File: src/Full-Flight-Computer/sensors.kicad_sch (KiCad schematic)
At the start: 11 parts, among them U12 BMM150, U3 BMI323, U5 BMP390

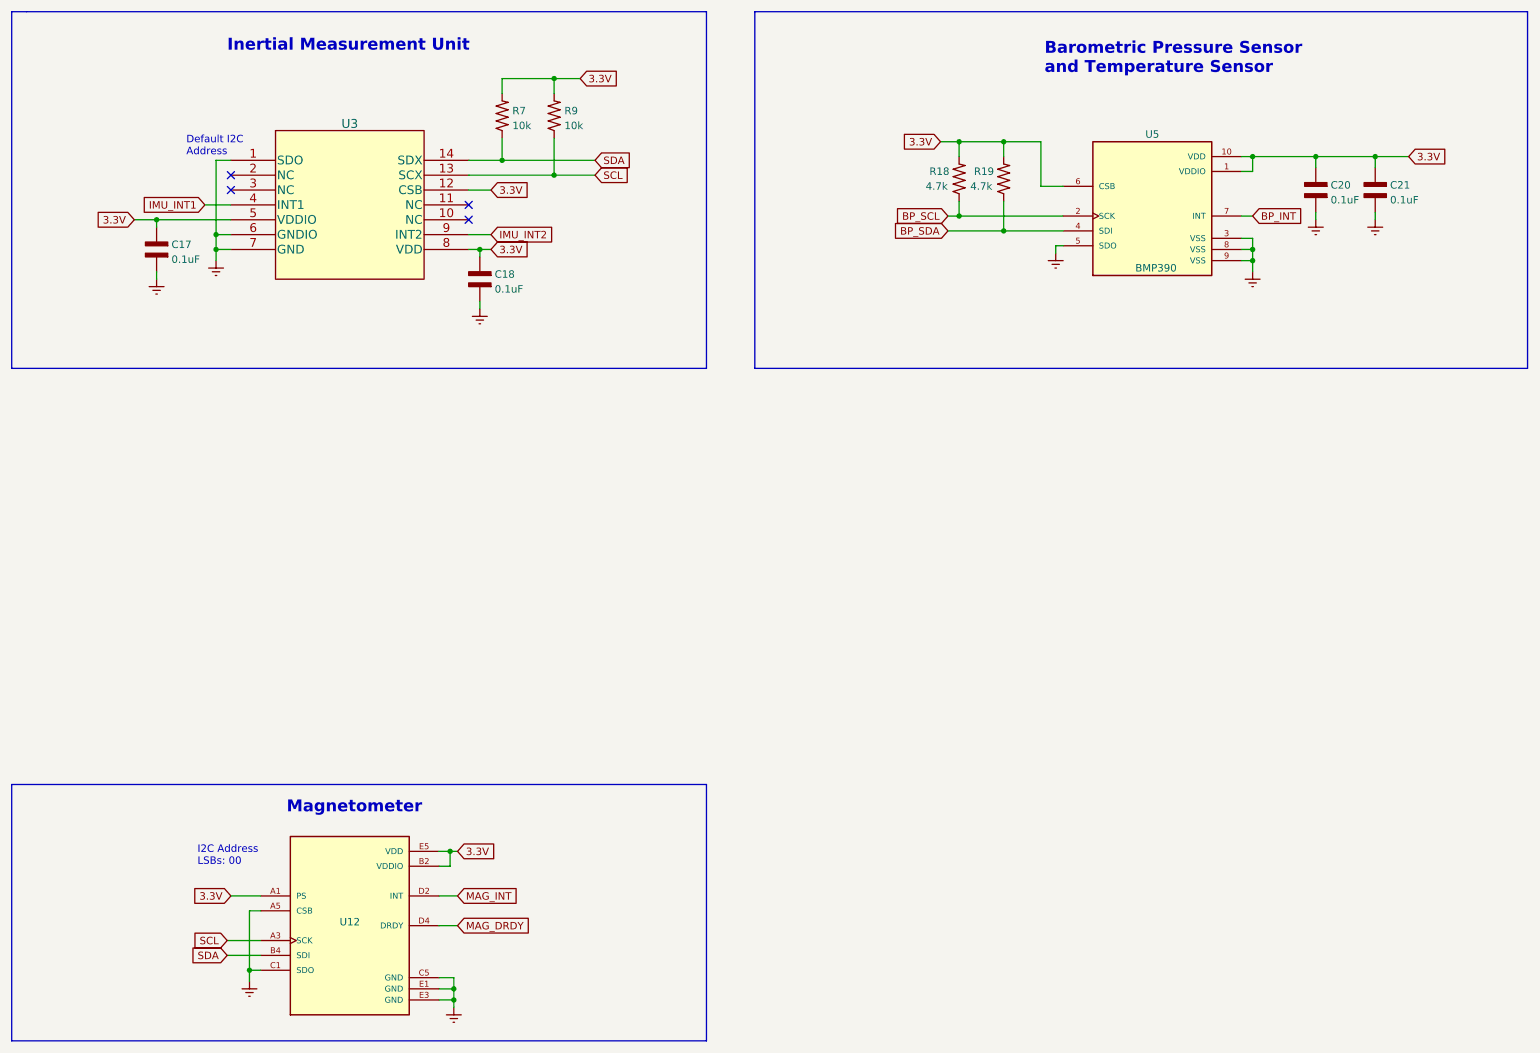
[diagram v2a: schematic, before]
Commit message: added auxiliary ports for staging/redundant ejection charges
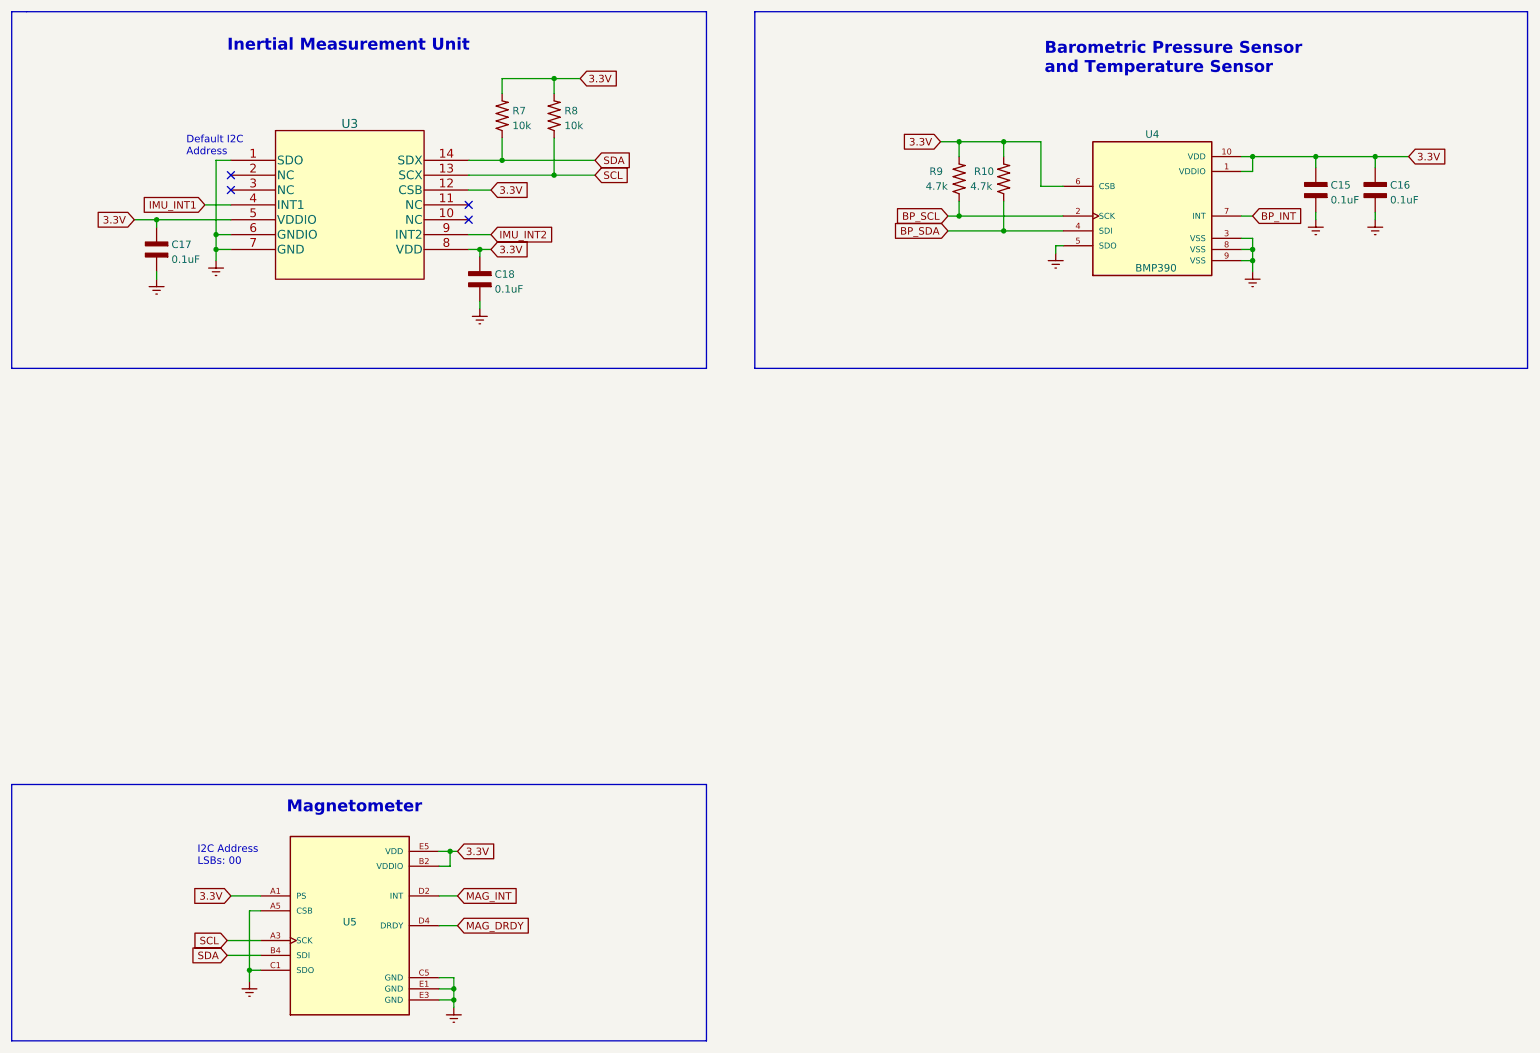
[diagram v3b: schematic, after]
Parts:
- renumbered C20 to C15, C21 to C16, R19 to R10, R9 to R8, R18 to R9, U5 to U4, U12 to U5

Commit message: implemented high G accelerometer schematic
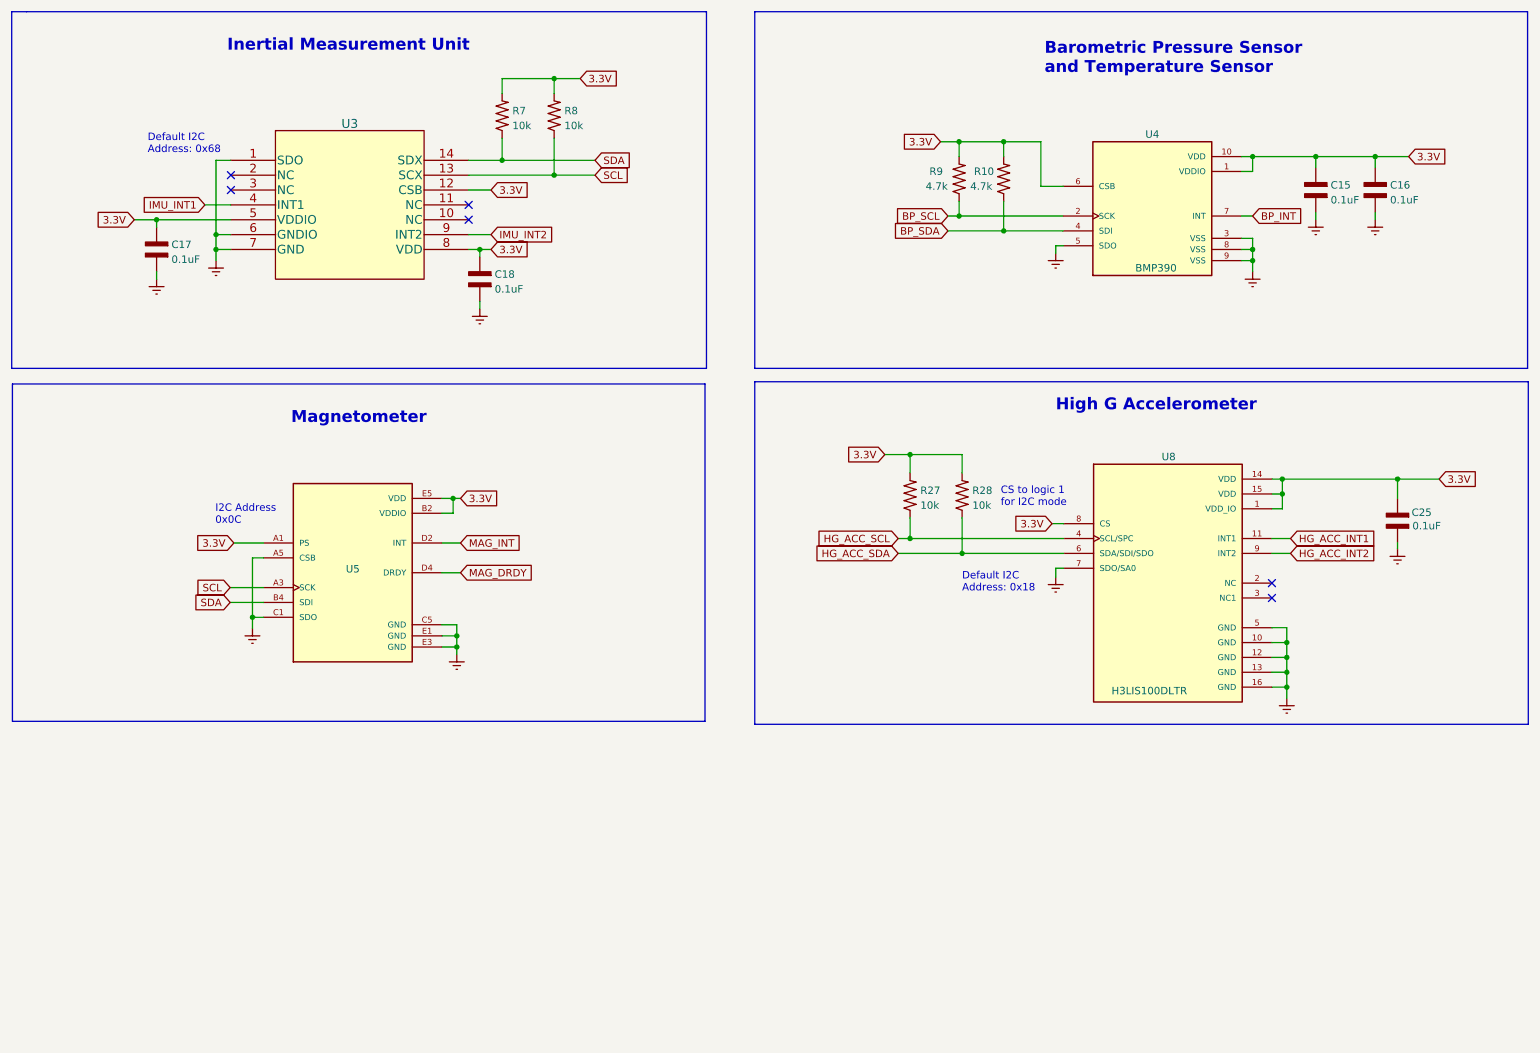
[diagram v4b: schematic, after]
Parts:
- added C25: 0.1uF, Full-Flight-Computer:CAP_0402, symbol Full-Flight-Computer:CAP_0402
- added R27, R28: 10k, Full-Flight-Computer:RES_0402, symbol Full-Flight-Computer:RES_0402
- added U8: H3LIS100DLTR, Full-Flight-Computer:H3LIS100DLTR, symbol Full-Flight-Computer:H3LIS100DLTR
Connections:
- net 3.3V: now also C25.1, R27.2, R28.2, U8.1 (VDD_IO), U8.14 (VDD), U8.15 (VDD), U8.8 (CS)
- net Earth: now also C25.2, U8.10 (GND), U8.12 (GND), U8.13 (GND), U8.16 (GND), U8.5 (GND), U8.7 (SDO/SA0)
- new net HG_ACC_INT1: U8.11 (INT1)
- new net HG_ACC_INT2: U8.9 (INT2)
- new net HG_ACC_SCL: R27.1, U8.4 (SCL/SPC)
- new net HG_ACC_SDA: R28.1, U8.6 (SDA/SDI/SDO)
- no-connect marks 4 -> 6
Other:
- note added: "CS to logic 1 for I2C mode"
- note added: "Default I2C Address: 0x18"
- note added: "Default I2C Address: 0x68"
- note added: "High G Accelerometer"
- note added: "I2C Address 0x0C"
- note removed: "Default I2C Address"
- note removed: "I2C Address LSBs: 00"
- moved on the sheet: U5

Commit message: redid component designators and updated BOM
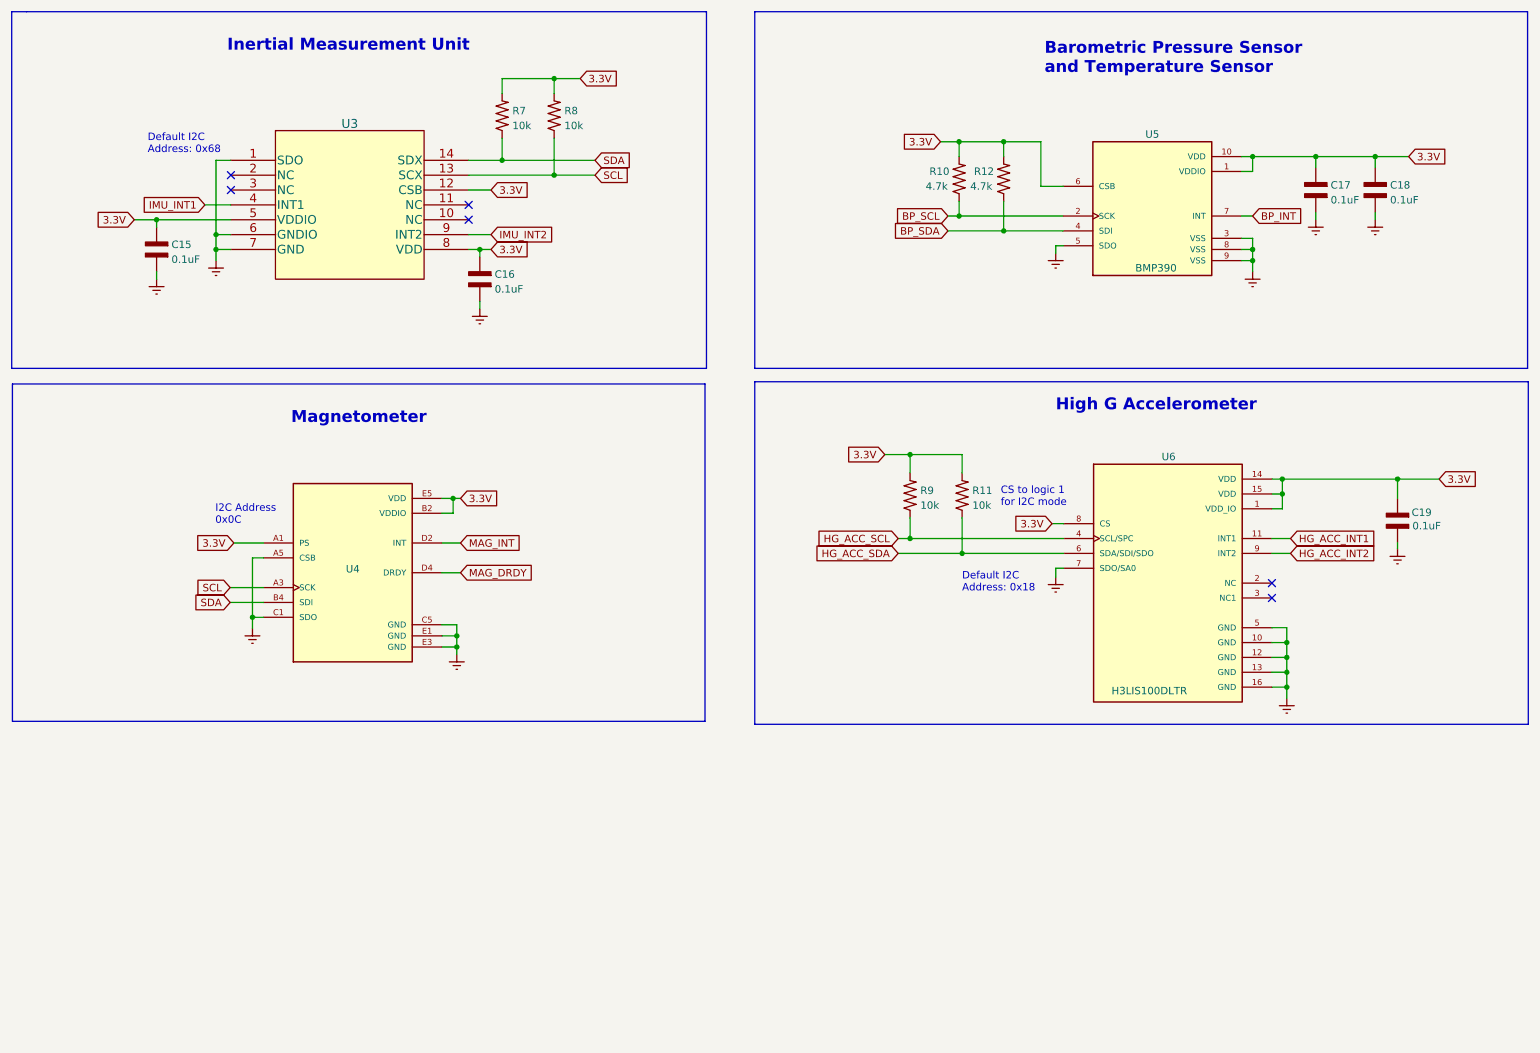
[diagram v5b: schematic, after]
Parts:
- renumbered C17 to C15, C18 to C16, C15 to C17, C16 to C18, C25 to C19, R9 to R10, R28 to R11, R10 to R12, R27 to R9, U5 to U4, U4 to U5, U8 to U6

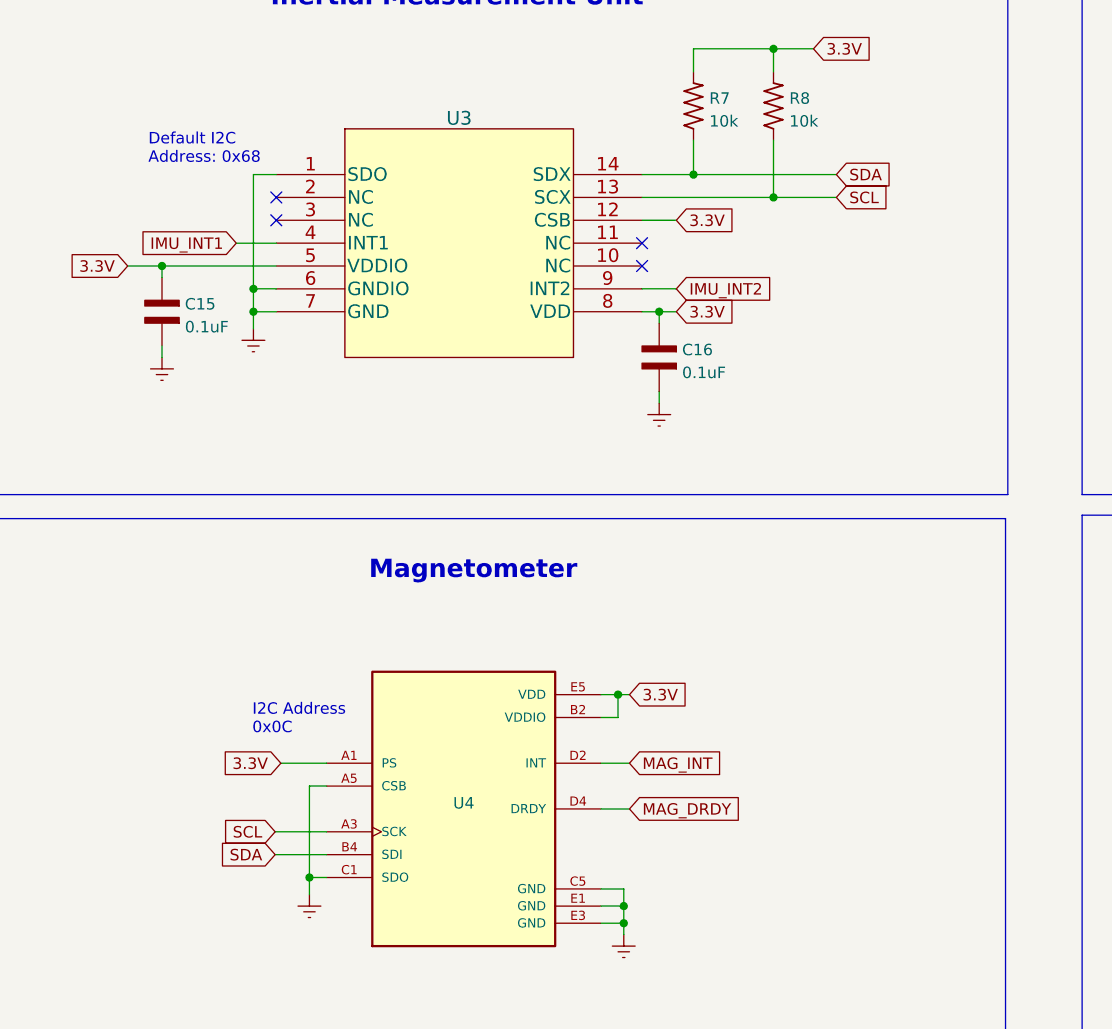
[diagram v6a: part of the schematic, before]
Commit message: add IMU prefix to IMU SDA and SCL labels
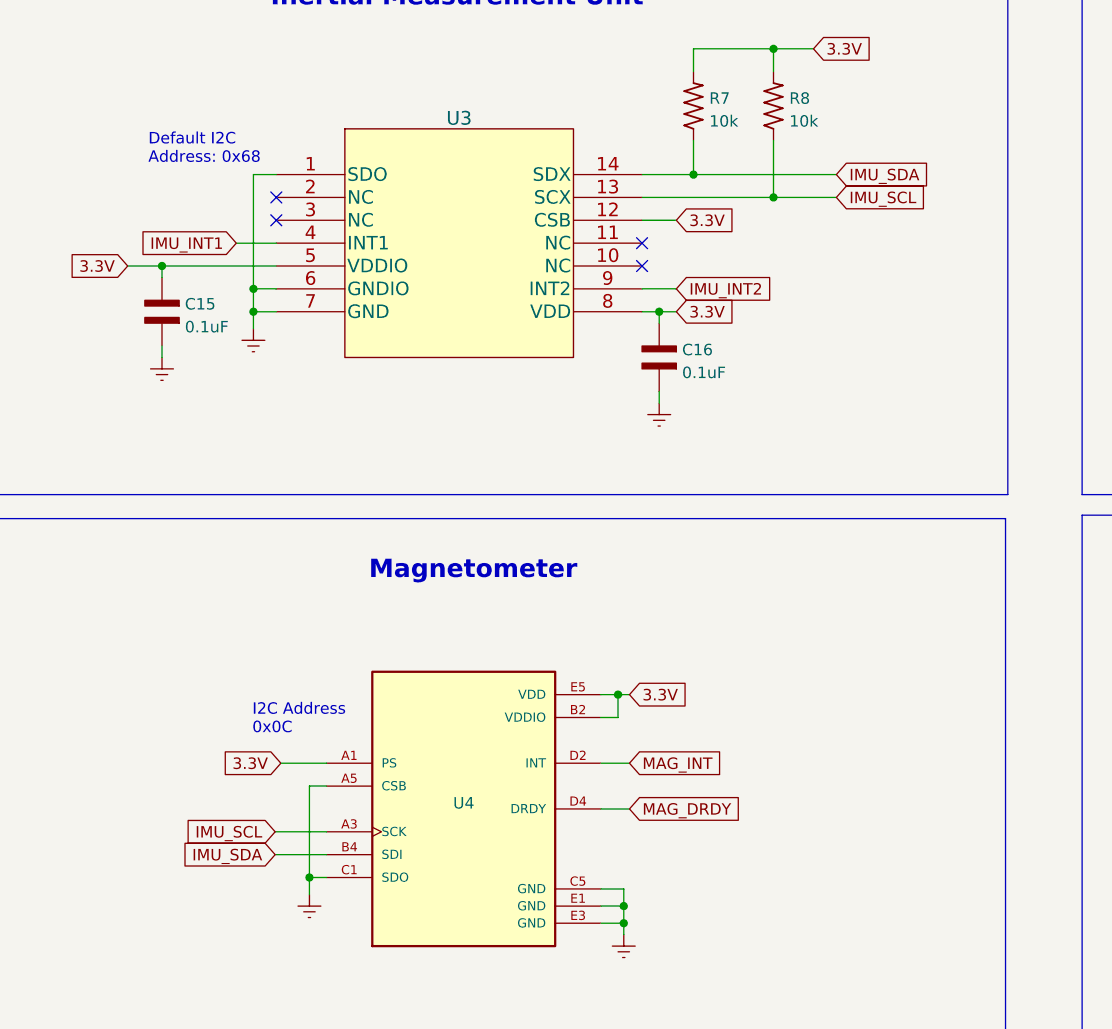
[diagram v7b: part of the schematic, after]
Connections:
- net SCL renamed IMU_SCL
- net SDA renamed IMU_SDA
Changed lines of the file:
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@@
     )
   )
-  (global_label "SCL" (shape input) (at 118.11 45.72 0) (fields_autoplaced)
+  (global_label "IMU_SCL" (shape input) (at 118.11 45.72 0) (fields_autoplaced)
     (effects (font (size 1.27 1.27)) (justify left))
-    (property "Intersheetrefs" "${INTERSHEET_REFS}" (at 123.9418 45.7994 0)
+    (property "Intersheetrefs" "${INTERSHEET_REFS}" (at 128.2235 45.72 0)
       (effects (font (size 1.27 1.27)) (justify left) hide)
     )
@@
     )
   )
-  (global_label "SDA" (shape input) (at 118.11 43.18 0) (fields_autoplaced)
+  (global_label "IMU_SDA" (shape input) (at 118.11 43.18 0) (fields_autoplaced)
     (effects (font (size 1.27 1.27)) (justify left))
-    (property "Intersheetrefs" "${INTERSHEET_REFS}" (at 124.0023 43.2594 0)
+    (property "Intersheetrefs" "${INTERSHEET_REFS}" (at 128.284 43.18 0)
       (effects (font (size 1.27 1.27)) (justify left) hide)
     )
@@
     )
   )
-  (global_label "SCL" (shape input) (at 55.753 116.205 180) (fields_autoplaced)
+  (global_label "IMU_SCL" (shape input) (at 55.753 116.205 180) (fields_autoplaced)
     (effects (font (size 1.27 1.27)) (justify right))
-    (property "Intersheetrefs" "${INTERSHEET_REFS}" (at 49.9212 116.1256 0)
+    (property "Intersheetrefs" "${INTERSHEET_REFS}" (at 45.6395 116.205 0)
       (effects (font (size 1.27 1.27)) (justify right) hide)
     )
@@
     )
   )
-  (global_label "SDA" (shape input) (at 55.753 118.745 180) (fields_autoplaced)
+  (global_label "IMU_SDA" (shape input) (at 55.753 118.745 180) (fields_autoplaced)
     (effects (font (size 1.27 1.27)) (justify right))
-    (property "Intersheetrefs" "${INTERSHEET_REFS}" (at 49.8607 118.6656 0)
+    (property "Intersheetrefs" "${INTERSHEET_REFS}" (at 45.579 118.745 0)
       (effects (font (size 1.27 1.27)) (justify right) hide)
     )
